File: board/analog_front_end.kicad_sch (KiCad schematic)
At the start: 42 parts, among them J9 731000105, U10 LMH6629, U11 OPA820, U12 DAC5571, U13 LM4040DBZ-2.0, U14 TLV3501, U15 DAC5571, U16 TLV9101, U8 OPA354, U9 ADG621

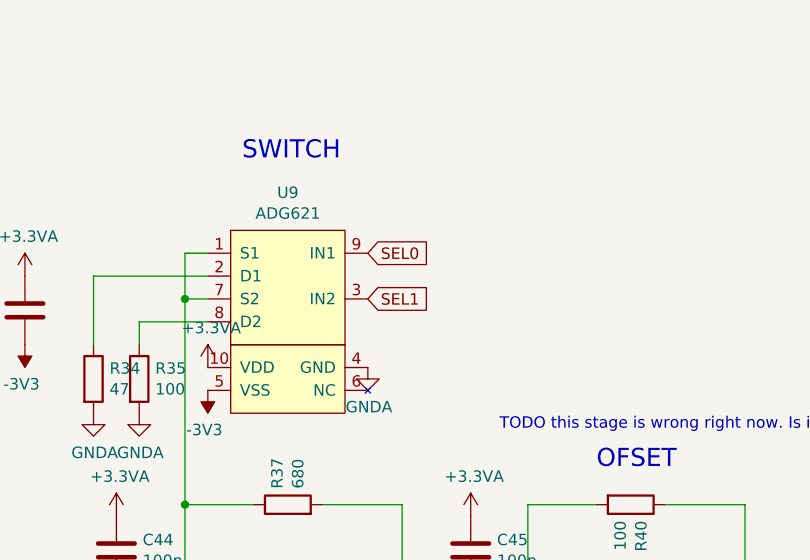
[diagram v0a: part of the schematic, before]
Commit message: More work on front end circuit, and GPIO connections
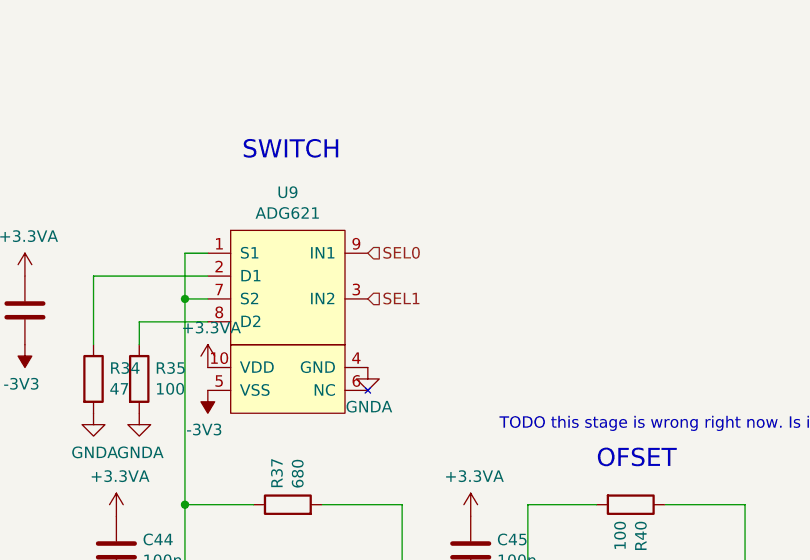
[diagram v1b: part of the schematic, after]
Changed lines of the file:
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@@
 		)
 	)
-	(global_label "SEL0"
+	(hierarchical_label "SEL0"
 		(shape input)
 		(at 179.07 76.2 0)
-		(fields_autoplaced yes)
 		(effects
 			(font
@@
 			(justify left)
 		)
-		(property "Intersheetrefs" "${INTERSHEET_REFS}"
-			(at 185.9971 76.2 0)
-			(effects
-				(font
-					(size 1.27 1.27)
-				)
-				(justify left)
-				(hide yes)
-			)
-		)
 	)
-	(global_label "SEL1"
+	(hierarchical_label "SEL1"
 		(shape input)
 		(at 179.07 81.28 0)
-		(fields_autoplaced yes)
 		(effects
 			(font
@@
 			(justify left)
 		)
-		(property "Intersheetrefs" "${INTERSHEET_REFS}"
-			(at 185.9971 81.28 0)
-			(effects
-				(font
-					(size 1.27 1.27)
-				)
-				(justify left)
-				(hide yes)
-			)
-		)
 	)

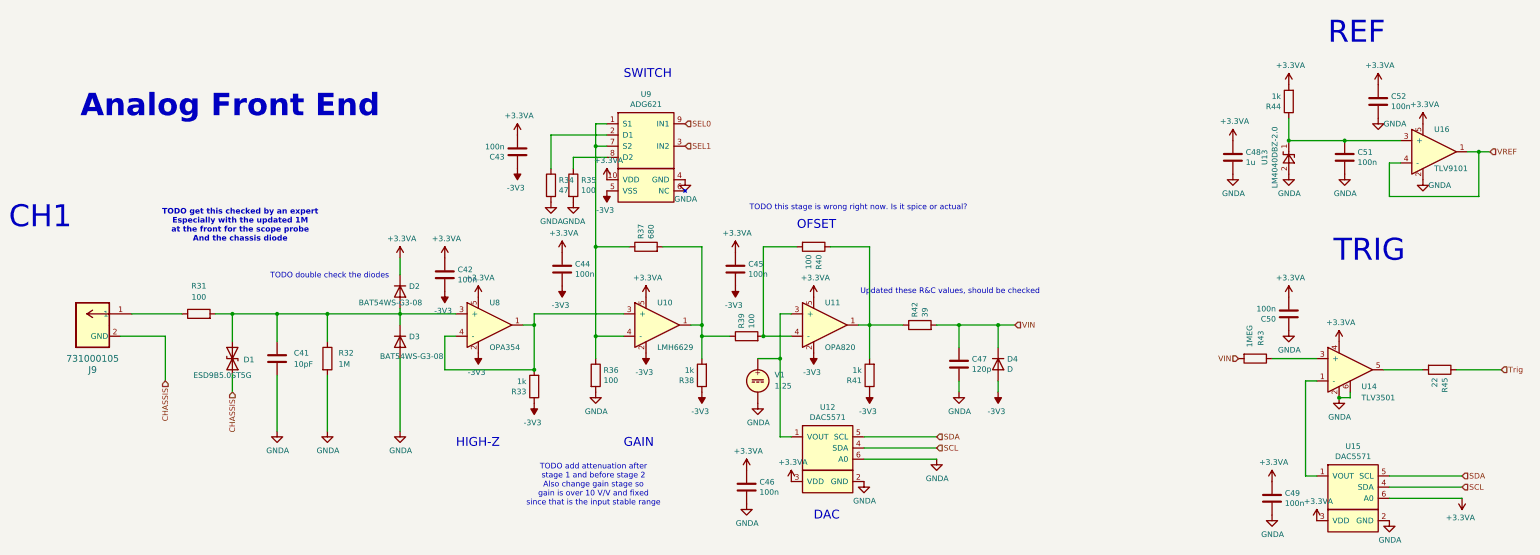
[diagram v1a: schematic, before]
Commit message: All components in layout
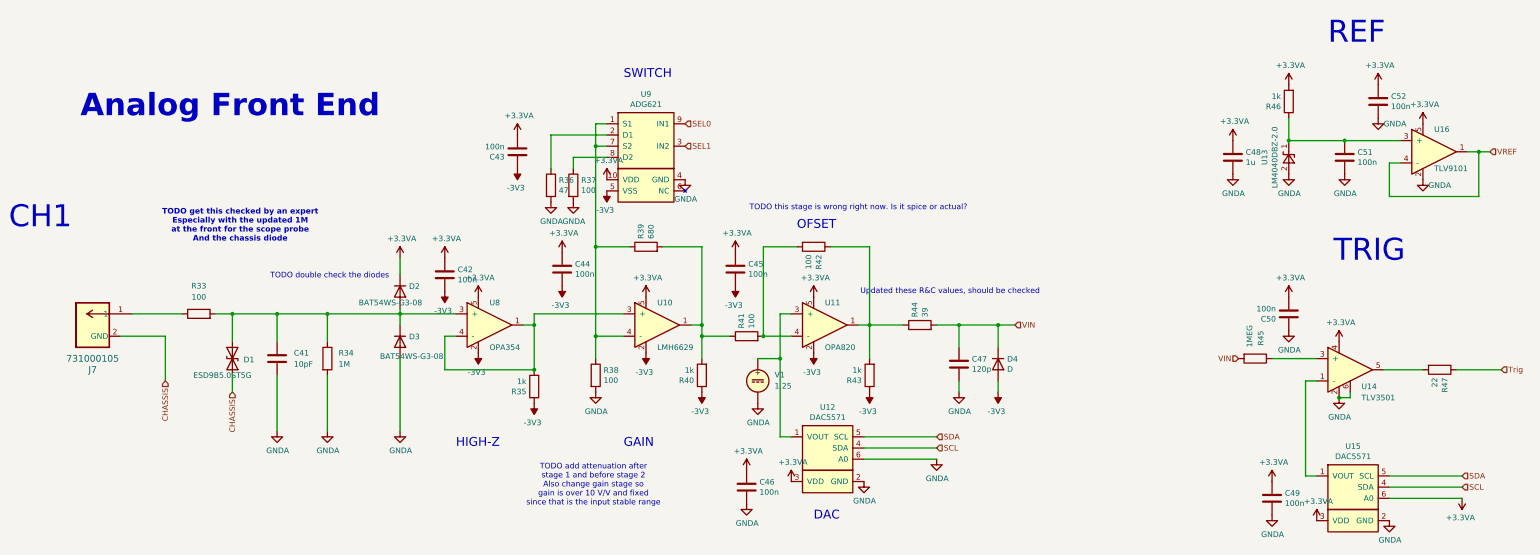
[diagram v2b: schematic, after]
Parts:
- C41: footprint (none) -> Capacitor_SMD:C_0603_1608Metric; MRF. Part # (none) -> C0603C100J5GACTU
- J7: renamed from J9; footprint CONN_73100-0105_MOL -> Footprints:CONN_73100-0105_MOL
- R33: renamed from R31; footprint (none) -> Resistor_SMD:R_0603_1608Metric; MRF. Part # (none) -> RC0603FR-0710KL
- R34: renamed from R32; footprint (none) -> Resistor_SMD:R_0603_1608Metric; MRF. Part # (none) -> RC0603FR-071ML
- V1: now left out of the parts list
- renumbered R33 to R35, R34 to R36, R35 to R37, R36 to R38, R37 to R39, R38 to R40, R39 to R41, R40 to R42, R41 to R43, R42 to R44, R43 to R45, R44 to R46, R45 to R47

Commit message: Added battery JST connector
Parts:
- C41: MFR. Part # (none) -> C0603C100J5GACTU; MRF. Part # C0603C100J5GACTU -> (none)
- R33: MFR. Part # (none) -> RC0603FR-0710KL; MRF. Part # RC0603FR-0710KL -> (none)
- R34: MFR. Part # (none) -> RC0603FR-071ML; MRF. Part # RC0603FR-071ML -> (none)
- U16: MFR. Part # (none) -> TLV9101IDBVR; MRF. Part # TLV9101IDBVR -> (none)
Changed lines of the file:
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@@
 			)
 		)
-		(property "MRF. Part #" "TLV9101IDBVR"
+		(property "MRF. Part #" ""
+			(at 341.63 76.2 0)
+			(effects
+				(font
+					(size 1.27 1.27)
+				)
+				(hide yes)
+			)
+		)
+		(property "MFR. Part #" "TLV9101IDBVR"
 			(at 341.63 76.2 0)
 			(effects
@@
 			)
 		)
-		(property "MRF. Part #" "C0603C100J5GACTU"
+		(property "MRF. Part #" ""
+			(at 86.36 129.54 0)
+			(effects
+				(font
+					(size 1.27 1.27)
+				)
+				(hide yes)
+			)
+		)
+		(property "MFR. Part #" "C0603C100J5GACTU"
 			(at 86.36 129.54 0)
 			(effects
@@
 			)
 		)
-		(property "MRF. Part #" "RC0603FR-071ML"
+		(property "MRF. Part #" ""
+			(at 97.79 129.54 0)
+			(effects
+				(font
+					(size 1.27 1.27)
+				)
+				(hide yes)
+			)
+		)
+		(property "MFR. Part #" "RC0603FR-071ML"
 			(at 97.79 129.54 0)
 			(effects
@@
 			)
 		)
-		(property "MRF. Part #" "RC0603FR-0710KL"
+		(property "MRF. Part #" ""
+			(at 68.58 119.38 90)
+			(effects
+				(font
+					(size 1.27 1.27)
+				)
+				(hide yes)
+			)
+		)
+		(property "MFR. Part #" "RC0603FR-0710KL"
 			(at 68.58 119.38 90)
 			(effects

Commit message: Production version of board
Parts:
- D1: MFR. Part # (none) -> ESD9B5.0ST5G
- D2, D3: MFR. Part # (none) -> BAT54WS-E3-08
- D4: now not fitted; now left out of the parts list
- J7: MFR. Part # (none) -> 731000105
- R33: MFR. Part # RC0603FR-0710KL -> ERJ-3EKF1000V
- R37, R38, R41, R42: MFR. Part # 0603WAF1000T5E -> ERJ-3EKF1000V
- U10: MFR. Part # (none) -> LMH6629MFX/NOPB
- U12, U15: MFR. Part # (none) -> DAC5571IDBVT
- U14: MFR. Part # (none) -> TLV3501AIDBVT
- U9: MFR. Part # (none) -> ADG621BRMZ

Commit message: Started work on fixing PCB bugs
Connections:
- net SCL: now also U12.5 (SCL), U15.5 (SCL); no longer U12.4 (SDA), U15.4 (SDA)
- net SDA: now also U12.4 (SDA), U15.4 (SDA); no longer U12.5 (SCL), U15.5 (SCL)
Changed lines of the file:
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@@
-		)
-	)
-	(hierarchical_label "SCL"
-		(shape input)
-		(at 355.6 158.75 0)
-		(effects
-			(font
-				(size 1.27 1.27)
-			)
-			(justify left)
 		)
 	)
@@
 		)
 	)
+	(hierarchical_label "SCL"
+		(shape input)
+		(at 236.22 147.32 0)
+		(effects
+			(font
+				(size 1.27 1.27)
+			)
+			(justify left)
+		)
+	)
 	(hierarchical_label "VREF"
 		(shape input)
 		(at 361.95 82.55 0)
+		(effects
+			(font
+				(size 1.27 1.27)
+			)
+			(justify left)
+		)
+	)
+	(hierarchical_label "SDA"
+		(shape input)
+		(at 355.6 158.75 0)
 		(effects
 			(font
@@
 		)
 	)
-	(hierarchical_label "SDA"
-		(shape input)
-		(at 236.22 147.32 0)
-		(effects
-			(font
-				(size 1.27 1.27)
-			)
-			(justify left)
-		)
-	)
 	(hierarchical_label "SCL"
 		(shape input)
-		(at 236.22 149.86 0)
+		(at 355.6 156.21 0)
 		(effects
 			(font
@@
 	(hierarchical_label "SDA"
 		(shape input)
-		(at 355.6 156.21 0)
+		(at 236.22 149.86 0)
 		(effects
 			(font
